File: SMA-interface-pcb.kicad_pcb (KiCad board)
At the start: 2 copper layers, 100 x 100 mm, 90 parts, among them J1 Conn_01x02_Pin, J10 Conn_01x04_Pin, J11 Conn_01x04_Pin, J12 USB_A_Stacked, J13 Conn_Coaxial, J14 Conn_Coaxial, J15 USB_A_Stacked, J16 Conn_02x03_Odd_Even, J2 Conn_01x02_Pin, J3 Conn_01x02_Pin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

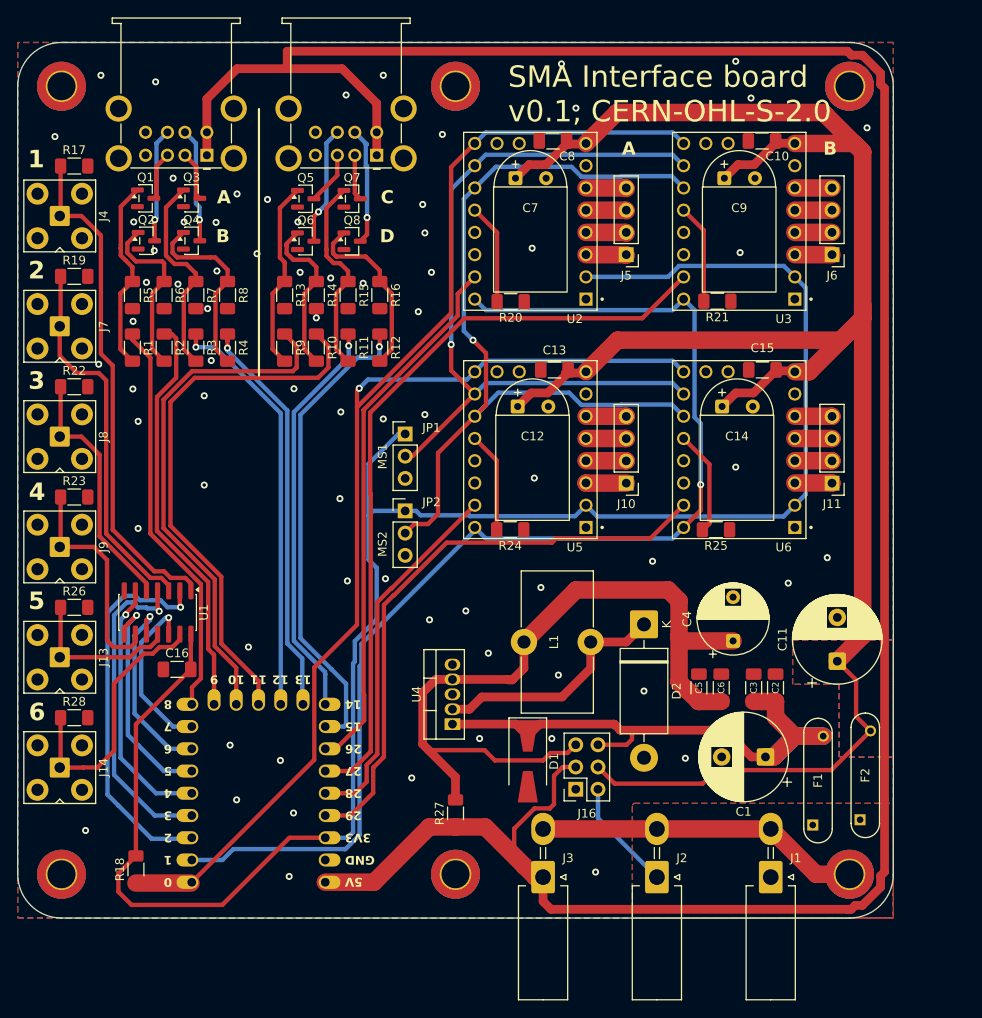
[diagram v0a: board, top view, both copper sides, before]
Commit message: rounded tracks, updated Library
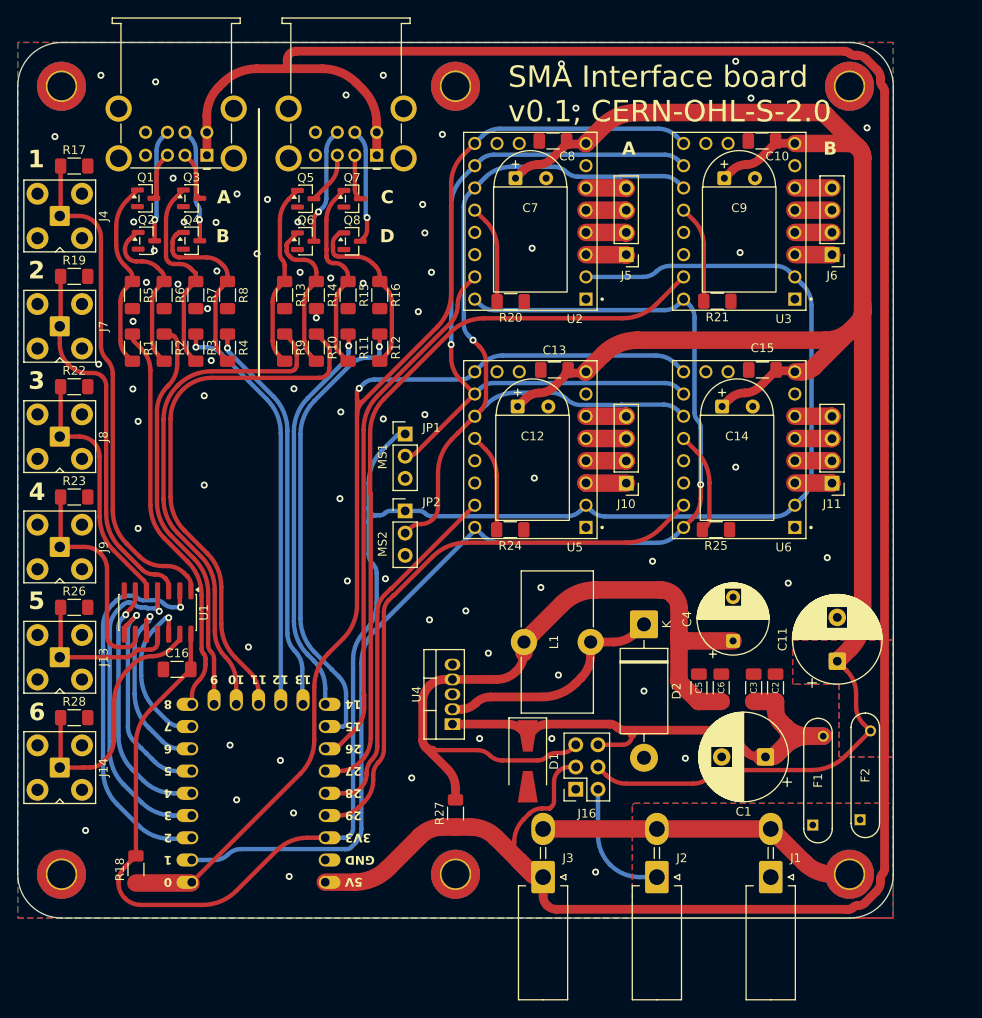
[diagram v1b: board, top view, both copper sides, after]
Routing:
- net /24V_protected: track 66.1 -> 69.1 mm
- net /5V_main: track 288.1 -> 285.3 mm
- net /MS2: track 97.8 -> 95.7 mm
- net /24V_motor: track 231.5 -> 229.5 mm
- net /24V_input: track 12.8 -> 14.7 mm
- net /Dout_light_C: track 59.4 -> 57.7 mm
- net Net-(D2-K): track 27.6 -> 26.1 mm
- net /Direction: track 138.4 -> 137.0 mm
- net /3.3V: track 215.4 -> 214.1 mm
- net /mot_step_D: track 67.3 -> 66.1 mm
- net /mot_step_B: track 86.8 -> 85.7 mm
- net /Dout_light_D: track 62.7 -> 61.7 mm
- net /Dout_light_B: track 47.0 -> 46.0 mm
- net /Dout_sound_D: track 54.3 -> 53.4 mm
- net /MS1: track 89.2 -> 88.4 mm
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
